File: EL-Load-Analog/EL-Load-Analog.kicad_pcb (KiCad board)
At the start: 4 copper layers, 185 x 95 mm, 295 parts, among them J1 Temp Sensor PCB, J2 SWEB8094AU-SW, J3 Conn_02x06_Odd_Even, J4 Conn_02x08_Odd_Even, J5 SWEB8094AU-RT, J7 Conn_01x02_Socket, J8 Conn_02x08_Odd_Even, J9 Temp Sensor heatsink, K2 EE2-5TNU, Q1 2N7002, Q101 TIP42C, Q2 2N7002, Q201 2N7002, Q202 2N7002, Q203 IRFP250M, Q204 IRFP250M, Q205 2N7002, Q206 2N7002, Q207 IRFP250M, Q208 IRFP250M, Q3 MMBT5551, Q301 2N7002, Q4 MMBT3904, Q5 MMBT5401, Q6 MMBT5551, U1 SN74LVC1G3157DBV, U10 TL072/OPA2376, U11 DAC8555, U12 DAC8555, U15 TPS7A2030, U17 TPS72325, U18 MCP6V51, U19 MCP6V51, U20 ADS131M02, U201 LM318D, U202 LM318D, U203 MCP6V51/LTC2050HV, U204 MCP6V51/LTC2050HV, U205 LM318D, U206 LM318D, U207 MCP6V51/LTC2050HV, U208 MCP6V51/LTC2050HV, U21 LT1964-5, U22 AMS1117, U23 TLV1117-50, U301 LM833, U302 LM833, U303 OPA189/MCP6V51/LTC2050HV, U304 OPA189/MCP6V51/LTC2050HV, U305 74HCT02, U306 LM393, U4 REF5025AD, U401 AD8038, U402 LM393, U403 74HCT02, U5 24LC32, U8 VO1400AEFTR, U9 VO1400AEFTR, X3 DIB Pheriperal connector

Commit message: Final v3C version for Analog PCB.
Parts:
- C401: value 670n -> 680n
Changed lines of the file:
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@@
     (descr "Capacitor SMD 0805 (2012 Metric), square (rectangular) end terminal, IPC_7351 nominal, (Body size source: IPC-SM-782 page 76, https://www.pcb-3d.com/wordpress/wp-content/uploads/ipc-sm-782a_amendment_1_and_2.pdf, https://docs.google.com/spreadsheets/d/1BsfQQcO9C6DZCsRaXUlFlo91Tg2WpOkGARC1WS5S8t0/edit?usp=sharing), generated with kicad-footprint-generator")
     (tags "capacitor")
-    (property "Part Name" "C_2.2uF_10V_X7R_10%_0805")
+    (property "Part Name" "C_2.2uF_25V_X7R_10%_0805")
     (property "Sheetfile" "Monitoring.kicad_sch")
     (property "Sheetname" "Monitoring, Crossover, Von")
@@
     (descr "Capacitor SMD 0805 (2012 Metric), square (rectangular) end terminal, IPC_7351 nominal, (Body size source: IPC-SM-782 page 76, https://www.pcb-3d.com/wordpress/wp-content/uploads/ipc-sm-782a_amendment_1_and_2.pdf, https://docs.google.com/spreadsheets/d/1BsfQQcO9C6DZCsRaXUlFlo91Tg2WpOkGARC1WS5S8t0/edit?usp=sharing), generated with kicad-footprint-generator")
     (tags "capacitor")
-    (property "Part Name" "C_2.2uF_10V_X7R_10%_0805")
+    (property "Part Name" "C_2.2uF_25V_X7R_10%_0805")
     (property "Sheetfile" "shifts-refs.kicad_sch")
     (property "Sheetname" "Power & References")
@@
     (descr "Capacitor SMD 0805 (2012 Metric), square (rectangular) end terminal, IPC_7351 nominal, (Body size source: IPC-SM-782 page 76, https://www.pcb-3d.com/wordpress/wp-content/uploads/ipc-sm-782a_amendment_1_and_2.pdf, https://docs.google.com/spreadsheets/d/1BsfQQcO9C6DZCsRaXUlFlo91Tg2WpOkGARC1WS5S8t0/edit?usp=sharing), generated with kicad-footprint-generator")
     (tags "capacitor")
+    (property "Part Name" "C_680nF_25V_X7R_10%_0805")
     (property "Sheetfile" "cv-von.kicad_sch")
     (property "Sheetname" "CV, OVP & OCP")
@@
         (effects (font (size 0.8 0.8) (thickness 0.15)))
     )
-    (fp_text value "670n" (at 0 1.68) (layer "F.Fab")
+    (fp_text value "680n" (at 0 1.68) (layer "F.Fab")
         (effects (font (size 1 1) (thickness 0.15)))
     )
@@
     (descr "Capacitor SMD 0805 (2012 Metric), square (rectangular) end terminal, IPC_7351 nominal, (Body size source: IPC-SM-782 page 76, https://www.pcb-3d.com/wordpress/wp-content/uploads/ipc-sm-782a_amendment_1_and_2.pdf, https://docs.google.com/spreadsheets/d/1BsfQQcO9C6DZCsRaXUlFlo91Tg2WpOkGARC1WS5S8t0/edit?usp=sharing), generated with kicad-footprint-generator")
     (tags "capacitor")
-    (property "Part Name" "C_2.2uF_10V_X7R_10%_0805")
+    (property "Part Name" "C_2.2uF_25V_X7R_10%_0805")
     (property "Sheetfile" "shifts-refs.kicad_sch")
     (property "Sheetname" "Power & References")

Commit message: Working on #4,#2 fixed #8,#22
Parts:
- removed R39: 91, Resistor_SMD:R_0805_2012Metric
- C213, C214, C227, C228: value 470p -> 1n
- R18, R19: value 100k -> 470
- R203, R205, R223, R225: value 100k -> 22k
- R221, R222: value 10k -> 0
- R40: value 1k8 -> 200
- R41: value 220 -> 1k8
- moved R40 1.42 mm to (106.2, 72.5), turned to 90 degrees
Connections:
- R211 pad 2: GND -> GCOM
- R213 pad 2: GND -> GCOM
- R231 pad 2: GND -> GCOM
- R233 pad 2: GND -> GCOM
- R40 pad 1: Net-(R39-Pad2) -> +12V
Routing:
- net GCOM: track 143.2 -> 230.1 mm, vias 7 -> 8
- net GND: track 380.6 -> 366.8 mm
- net Net-(R225-Pad2): track 121.7 -> 124.5 mm, vias 3 -> 4
- net +5V: track 471.6 -> 474.2 mm
- net -5V: track 610.9 -> 613.2 mm
- net Net-(R39-Pad2): track 2.20 -> 0.00 mm

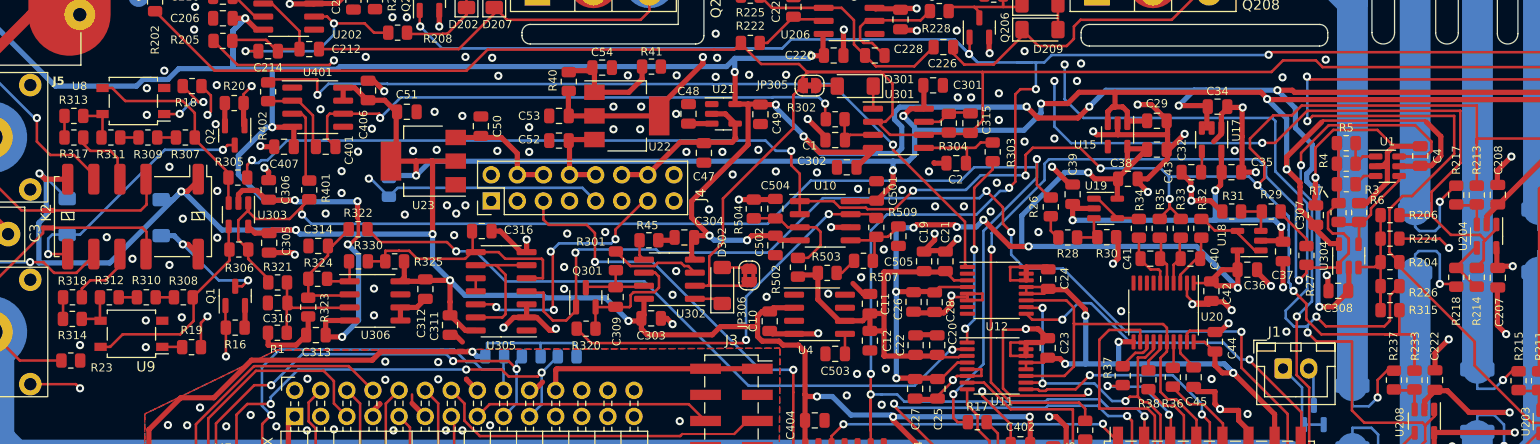
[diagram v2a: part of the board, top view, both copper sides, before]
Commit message: Fixing issues from #4, adding ESD protection (#6)
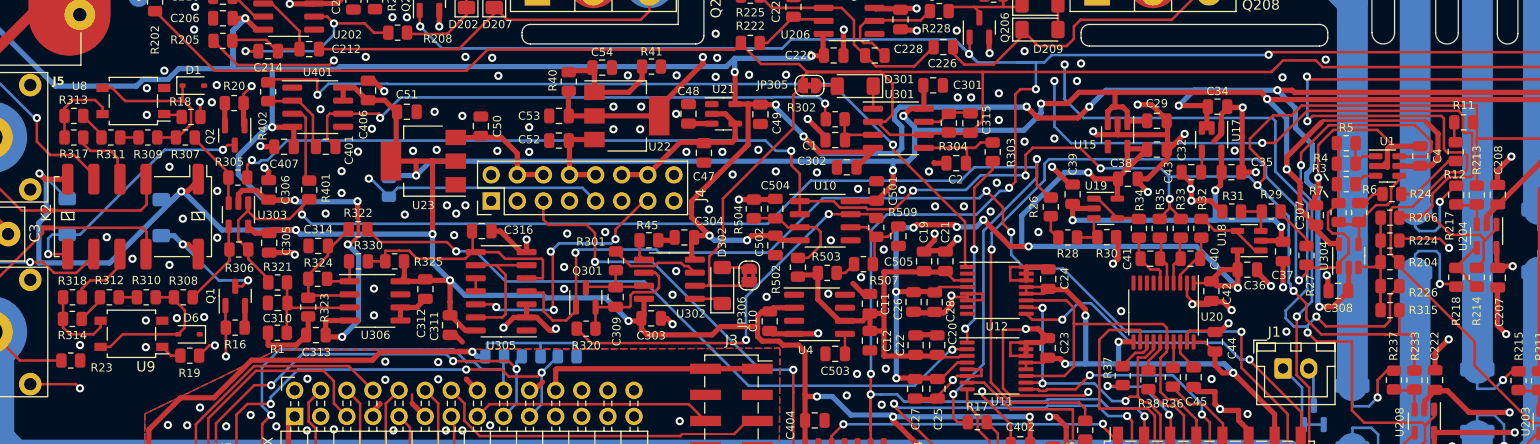
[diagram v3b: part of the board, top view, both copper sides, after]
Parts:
- added D1: PESD3V3L1BAF, Diode_SMD:D_SOD-323, F.Cu at (69.6, 72.8)
- added D6: PESD3V3L1BAF, Diode_SMD:D_SOD-323, F.Cu at (69.2, 97.0)
- added R11: 0, Resistor_SMD:R_0805_2012Metric, F.Cu at (193.2, 76.4)
- added R12: 0, Resistor_SMD:R_0805_2012Metric, F.Cu at (192.4, 79.3)
- added R24: 0, Resistor_SMD:R_0805_2012Metric, F.Cu at (186.2, 83.4)
- R27: value 100k 0.1% -> 10k 0.1%
- R29: value 10k 0.1% -> 100k 0.1%
- R307, R308: value 100k 0.1% -> 1k 0.1%
- R313, R314: value 39k 0.1% -> 100k 0.1%
- R317, R318: value 1k 0.1% -> 39k 0.1%
- moved R18 3.00 mm to (69.4, 75.9)
- moved R19 0.84 mm to (69.3, 99.1)
- moved R507 0.32 mm to (134.8, 90.2)
- moved R206 0.24 mm to (186.1, 85.7)
- moved R224 0.18 mm to (186.1, 87.9)
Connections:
- C505 pad 1: Net-(U10B-+) -> Net-(U10B--)
- R307 pad 2: Net-(R307-Pad2) -> Net-(D1-A1)
- R308 pad 1: Net-(R308-Pad1) -> Net-(D6-A2)
- R309 pad 1: Net-(R307-Pad2) -> Net-(D1-A1)
- R310 pad 2: Net-(R308-Pad1) -> Net-(D6-A2)
- R507 pad 2: Net-(U10B-+) -> Net-(U10B--)
- R509 pad 1: Net-(U10B-+) -> Net-(U10B--)
- R6 pad 1: GND -> Net-(R24-Pad1)
- U10 pad 5: Net-(U10B-+) -> GND
- U10 pad 6: GND -> Net-(U10B--)
- U8 pad 3: Net-(U303-+) -> Net-(D1-A1)
- U8 pad 4: Net-(R311-Pad2) -> Net-(R313-Pad2)
- U9 pad 3: Net-(R312-Pad1) -> Net-(R314-Pad1)
- U9 pad 4: Net-(U303--) -> Net-(D6-A2)
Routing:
- net Net-(D1-A1): track 0.00 -> 16.3 mm
- net Net-(D6-A2): track 0.00 -> 14.3 mm
- net Net-(U303-+): track 20.1 -> 7.75 mm
- net Net-(U303--): track 20.8 -> 8.53 mm
- net Net-(U10B--): track 0.00 -> 8.74 mm
- net Net-(U10B-+): track 7.69 -> 0.00 mm
- net Net-(R12-Pad1): track 0.00 -> 6.63 mm
- net GND: track 366.8 -> 360.2 mm, vias 235 -> 236
- net Net-(R314-Pad1): track 2.11 -> 8.12 mm
- net Net-(R313-Pad2): track 2.10 -> 8.10 mm
- net Net-(R18-Pad1): track 6.95 -> 1.82 mm, vias 2 -> 0
- net Net-(R24-Pad1): track 0.00 -> 3.34 mm
- net Net-(R203-Pad2): track 203.9 -> 206.6 mm
- net Net-(R205-Pad2): track 158.6 -> 160.8 mm
- net Net-(R11-Pad1): track 0.00 -> 1.86 mm
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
